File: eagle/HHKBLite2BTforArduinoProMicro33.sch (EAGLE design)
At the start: 42 parts, among them CON1 45045-1445, CON2 45045-0845, IC1 4514N, IC2 4512N, IC4 HT7733A, J1 J7MM, J2 J15MM, J3 J7MM, J4 J10MM

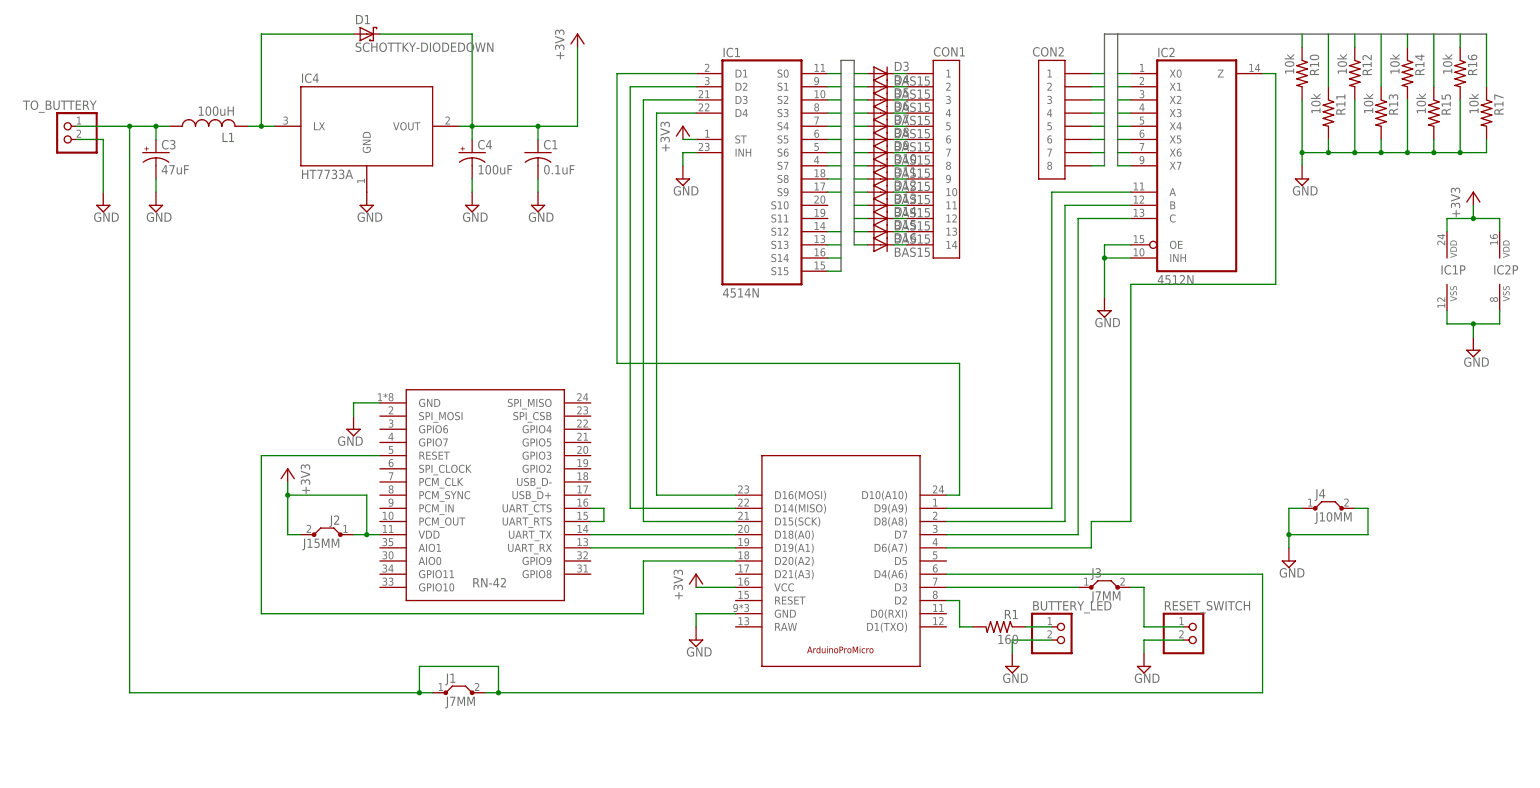
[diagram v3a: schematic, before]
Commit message: Arduino IDE 1.6.x のためにいろいろ変更.
Arduino IDE 1.6.x と Arduino-Makefile でこのプロジェクトをコンパイルできるように
するために, いろいろいじった.
まだ試験的なものなので, 今回変更した Makefile を参考にし, 他のものも
書き換えると良い.
あと, ProMicro33 に関して言えば, これをそのまま使ってもコンパイルできない.
SparkFun から適切なボードコンフィグを持ってきて, 適切な場所に置き,
適切に Makefile を書き換える必要がある.
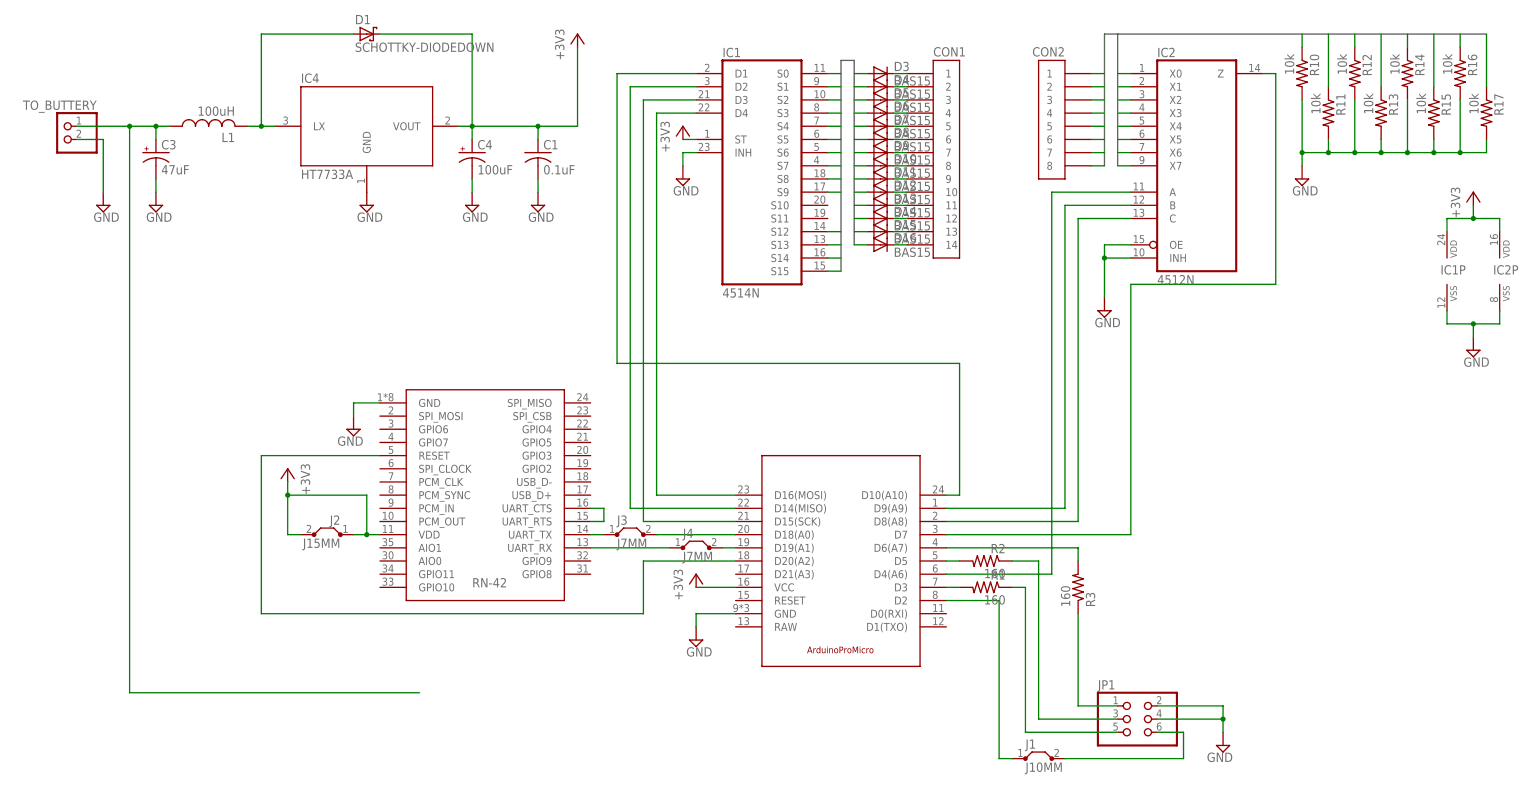
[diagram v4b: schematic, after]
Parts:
- removed BUTTERY_LED, RESET_SWITCH: (no value), pinhead:PINHD-1X2
- added JP1: (no value), pinhead:PINHD-2X3/90
- added R2: 160, rcl:R-US_0207/7
- added R3: 160, rcl:R-US_0207/10
- J1: value J7MM -> J10MM; device jumper:J7MM -> jumper:J10MM
- J4: value J10MM -> J7MM; device jumper:J10MM -> jumper:J7MM
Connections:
- new net N$10: JP1.3, R2.1
- new net N$11: JP1.5, R1.1
- new net N$12: J1.2, JP1.6
- new net N$13: J1.1, U$2.D2
- new net N$14: J4.1, U$1.UART_RX
- new net N$18: J4.2, U$2.D19(A1)
- net GND: now also JP1.2, JP1.4; no longer BUTTERY_LED.2, J4.1, J4.2, RESET_SWITCH.2
- net N$1: now also R3.2, U$2.D6(A7); no longer BUTTERY_LED.1, R1.1
- net N$16: now also U$2.D9(A9); no longer U$2.D8(A8)
- net N$17: now also U$2.D8(A8); no longer U$2.D7
- net N$2: now also U$2.D3; no longer U$2.D2
- net N$22: now also U$2.D4(A6); no longer U$2.D9(A9)
- net N$4: now also R2.2, U$2.D5; no longer J3.2, RESET_SWITCH.1
- net N$5: now also J3.1; no longer U$2.D18(A0)
- net N$7: now also J3.2, U$2.D18(A0); no longer U$1.UART_RX, U$2.D19(A1)
- net N$8: now also JP1.1, R3.1; no longer J3.1, U$2.D3
- net N$9: now also U$2.D7; no longer U$2.D6(A7)
- net VCC_SRC: no longer J1.1, J1.2, U$2.D4(A6)
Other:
- moved on the sheet: J1, J3, J4, R1
